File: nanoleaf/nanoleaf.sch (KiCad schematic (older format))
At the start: 29 parts, among them J1 Bootloader, J2 Conn_01x04_Male, J3 Conn_01x04_Male, J4 Conn_01x04_Male, U1 ATtiny85-20SU

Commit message: Atualização do micro na pcb
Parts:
- added 68R: R, symbol Device:R
- added D?: 1N4148, symbol Device:D
- added D? (x2): D_Zener, symbol Device:D_Zener
- added J?: USB_B_Mini, symbol Connector:USB_B_Mini
- added R?: 1k5, symbol Device:R
- added R?: 68R, symbol Device:R
- added SW?: SW_Push_Dual, symbol Switch:SW_Push_Dual
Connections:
- net +5V: now also D?.1 (K), R?.1
- net GND: now also D?.2 (A), D?.2 (A), J?.5 (GND), J?.6 (Shield), SW?.2
- net PB3: now also 68R.1
- net PB4: now also R?.1
- net PB5: now also SW?.1
- new net: D?.2 (A), J?.1 (VBUS)
- new net: D?.1 (K), J?.2 (D-), R?.2
- new net: 68R.2, D?.1 (K), J?.3 (D+), R?.2
- no-connect marks 0 -> 3
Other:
- moved on the sheet: C1, C2, C3, D1, D10, D11, D12, D13, D14, D15, D16, D17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

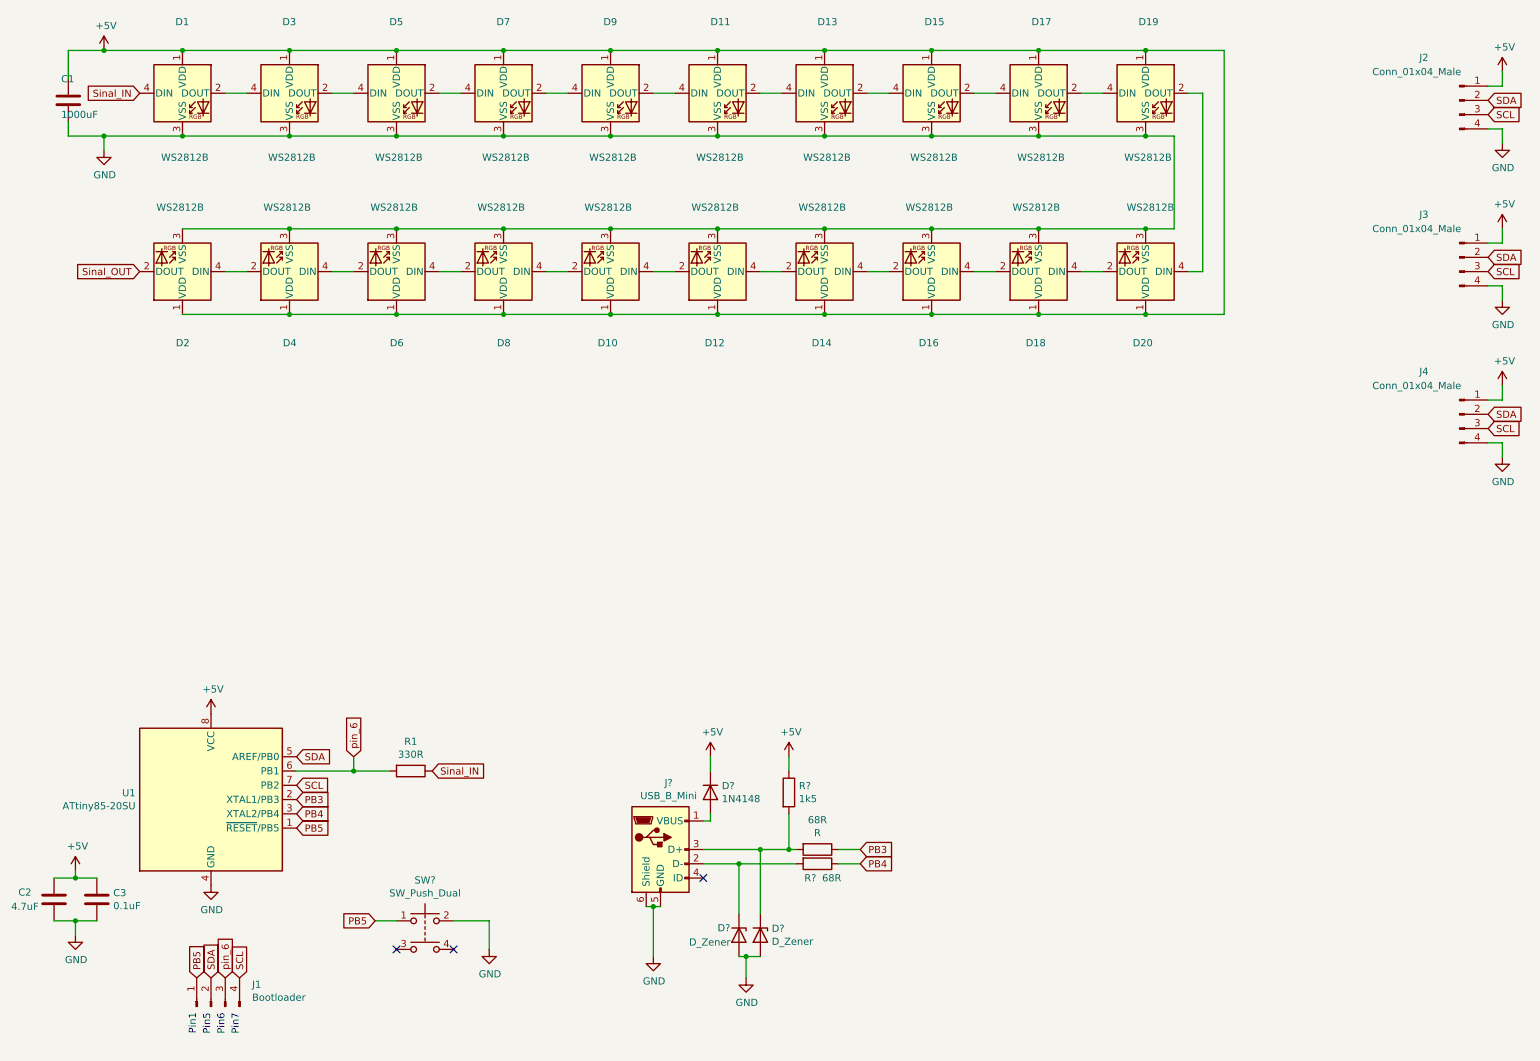
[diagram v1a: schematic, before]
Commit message: Upload do esquematico e primeira versão da pcb
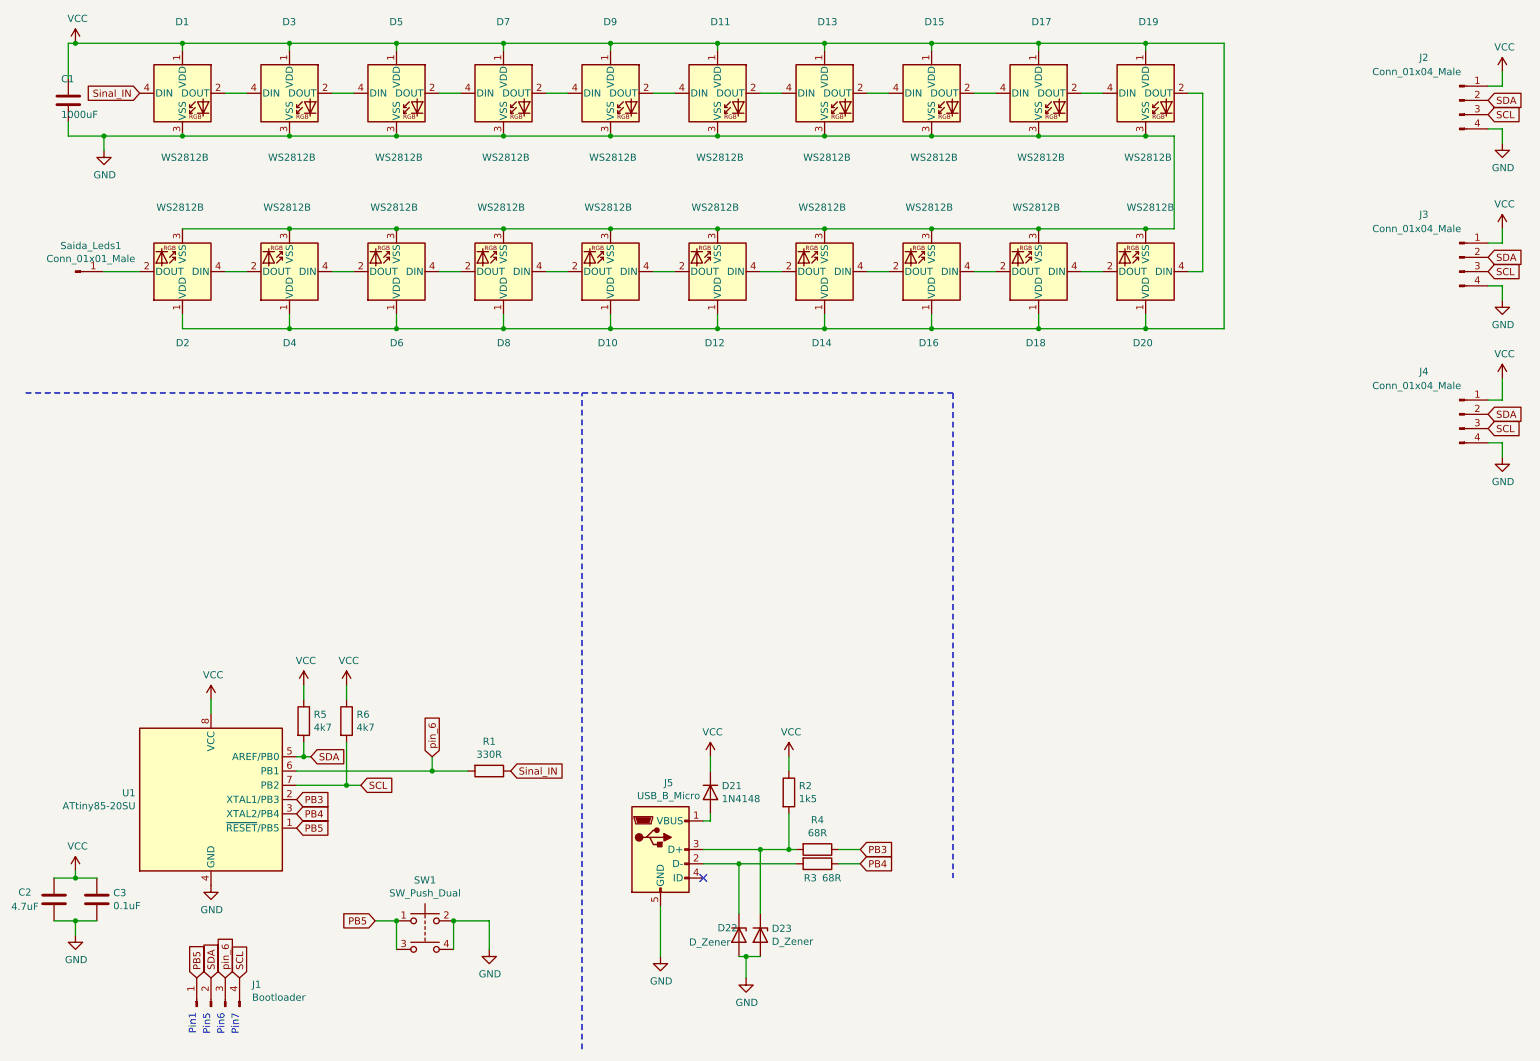
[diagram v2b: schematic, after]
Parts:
- removed J?: USB_B_Mini, symbol Connector:USB_B_Mini
- added J5: USB_B_Micro, Connector_USB:microusb, symbol Connector:USB_B_Micro
- added R5, R6: 4k7, Resistor_SMD:R_0805_2012Metric_Pad1.15x1.40mm_HandSolder, symbol Device:R
- added Saida_Leds1: Conn_01x01_Male, Connector_PinHeader_2.54mm:PinHeader_1x01_P2.54mm_Vertical, symbol Connector:Conn_01x01_Male
- C1, C2, C3: footprint (none) -> Capacitor_SMD:C_0805_2012Metric_Pad1.15x1.40mm_HandSolder
- D21, D22, D23: renamed from D?; footprint (none) -> Diode_SMD:D_0805_2012Metric_Pad1.15x1.40mm_HandSolder
- J1, J2, J3, J4: footprint (none) -> Connector_PinHeader_2.54mm:PinHeader_1x04_P2.54mm_Vertical
- R1: footprint (none) -> Resistor_SMD:R_0805_2012Metric_Pad1.15x1.40mm_HandSolder
- R2, R3: renamed from R?; footprint (none) -> Resistor_SMD:R_0805_2012Metric_Pad1.15x1.40mm_HandSolder
- R4: renamed from 68R; value R -> 68R; footprint (none) -> Resistor_SMD:R_0805_2012Metric_Pad1.15x1.40mm_HandSolder
- SW1: renamed from SW?; footprint (none) -> Button_Switch_THT:SW_1825910-6-4
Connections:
- net GND: now also SW1.4, J5.5 (GND)
- net PB5: now also SW1.3
- net SCL: now also R6.2
- net SDA: now also R5.2
- net at D21.2 (A): now also J5.1 (VBUS)
- net at D22.1 (K), R3.2: now also J5.2 (D-)
- net at D23.1 (K), R2.2, R4.2: now also J5.3 (D+)
- net +5V renamed VCC
- net VCC: now also R5.1, R6.1
- net Sinal_OUT: no longer names the net of D2.2 (DOUT)
- net Sinal_OUT: now also Saida_Leds1.1 (Pin_1)
- no-connect marks 3 -> 1
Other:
- moved on the sheet: R1
